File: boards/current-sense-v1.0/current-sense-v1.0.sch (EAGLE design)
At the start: 90 parts, among them IC1 ISO7241, IC2 ISO7241, IC3 ISO7242, IC4 ISO7240, J1 4-PIN_2MM-H, J2 MKS-1658, J3 8-PIN_2MM-H, J6 DF22-2, Q1 IRFH7545, Q2 IRFH7545, Q3 IRFH7545, Q4 IRFH7545, Q5 IRFH7545, Q6 IRFH7545, U1 DRV8303DCA, U13 TLV70233DBVR, U2 INA240PWR, U3 INA240PWR, U4 INA240PWR, U5 TLV70233DBVR, U6 ADS8028IRTJT, U7 MPM3620GQV-P, U8 VND5E006ASPTR-E, U9 TLV70450

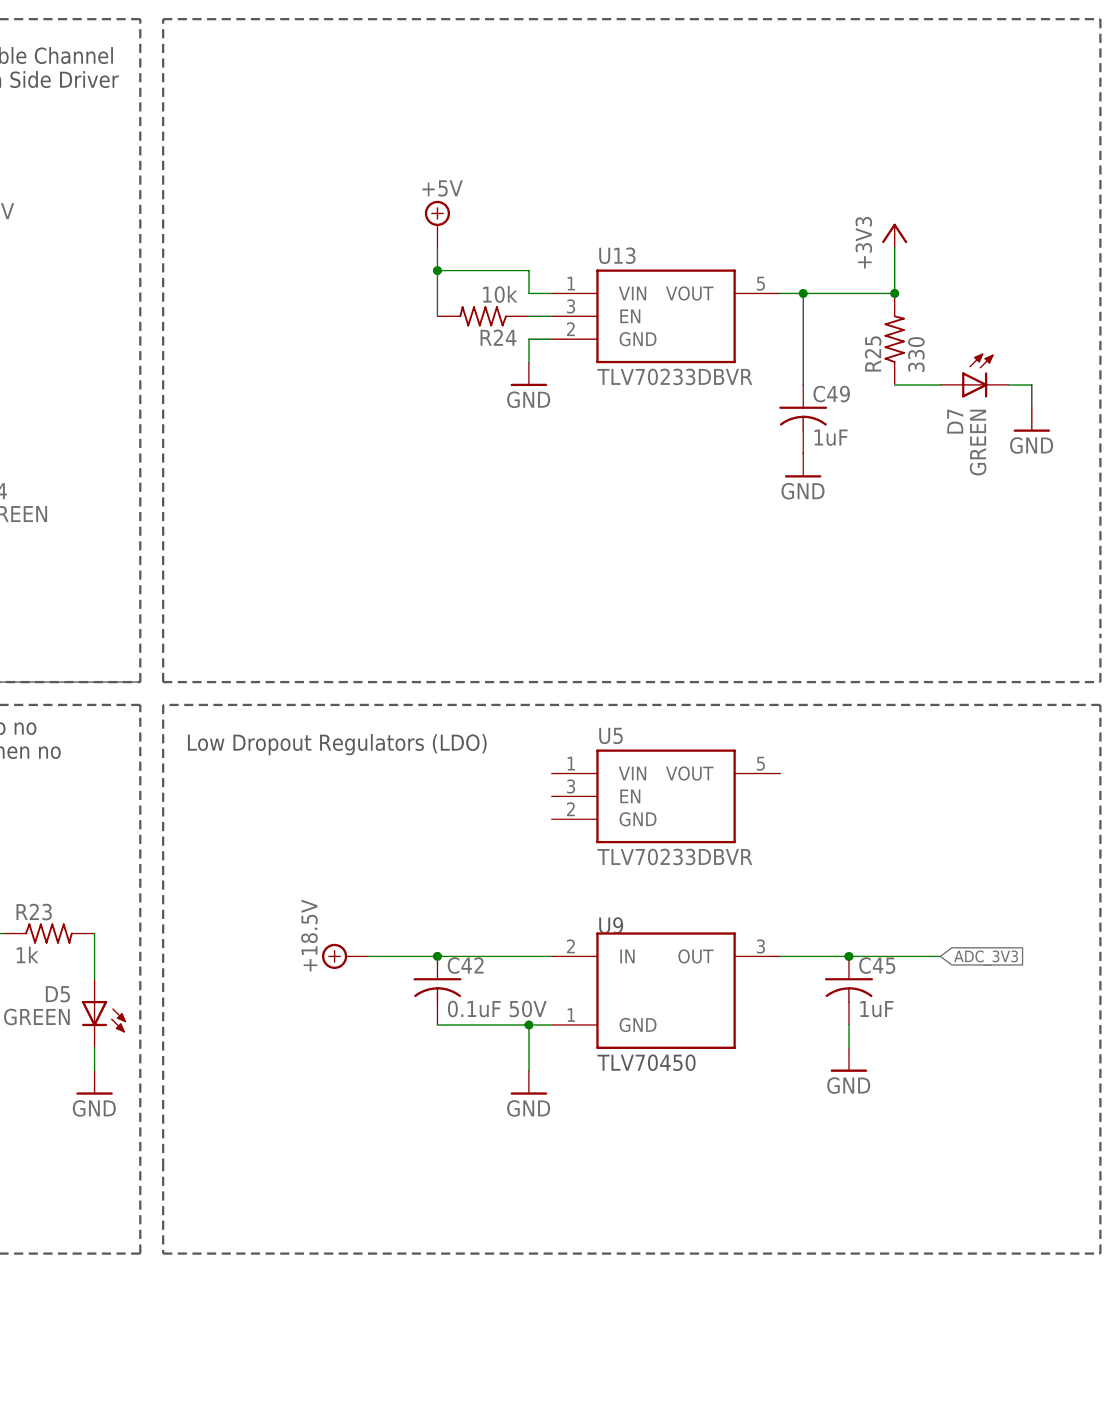
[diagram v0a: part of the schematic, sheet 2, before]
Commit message: replaced TLV 70450 with TLV 70433
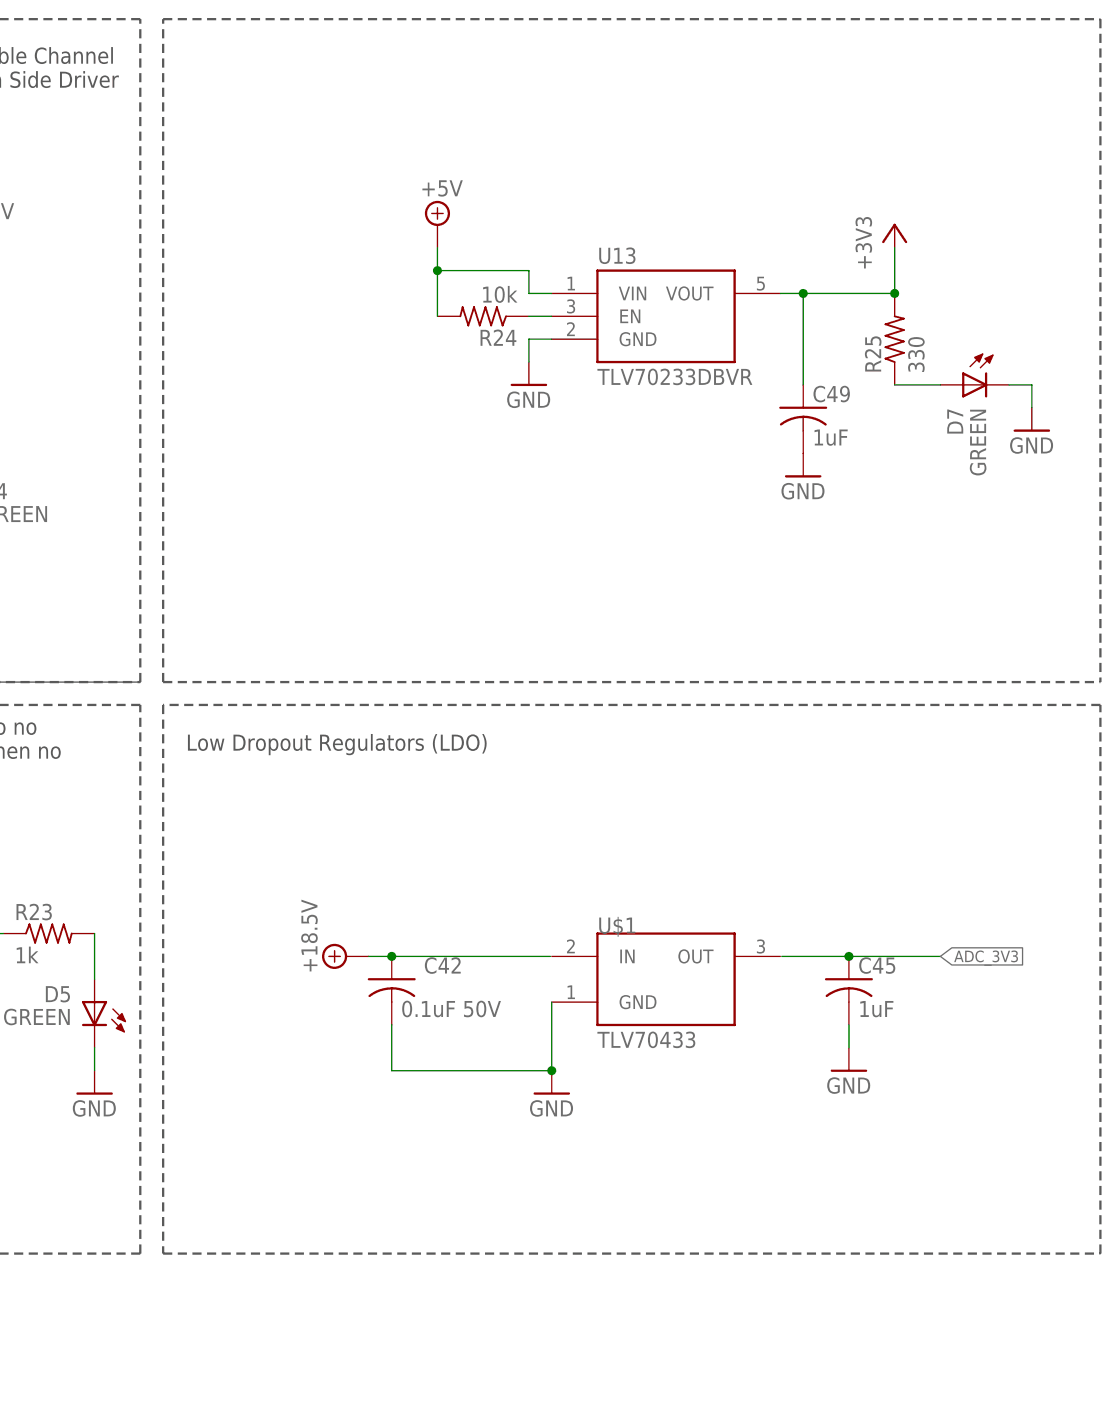
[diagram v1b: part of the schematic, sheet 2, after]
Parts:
- removed U5: TLV70233DBVR, RoboJackets-PowerICs:TLV70233DBVR
- removed U9: TLV70450, RoboJackets-PowerICs:TLV70450
- added U$1: TLV70433, RoboJackets-PowerICs:TLV70433
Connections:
- net +18.5V: no longer U9.IN
- net ADC_3V3: no longer U9.OUT
- net GND: now also U$1.GND; no longer U9.GND
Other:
- moved on the sheet: C42
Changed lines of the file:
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@@
 <part name="GND80" library="supply1" library_urn="urn:adsk.eagle:library:371" deviceset="GND" device=""/>
 <part name="SUPPLY42" library="RoboJackets-Supplies" deviceset="+18.5V" device=""/>
-<part name="U9" library="RoboJackets-PowerICs" deviceset="TLV70450" device=""/>
 <part name="C14" library="rcl" library_urn="urn:adsk.eagle:library:334" deviceset="C-US" device="C0603" package3d_urn="urn:adsk.eagle:package:23616/2" value="0.1uf"/>
 <part name="GND24" library="supply1" library_urn="urn:adsk.eagle:library:371" deviceset="GND" device=""/>
@@
 <part name="+3V13" library="supply1" library_urn="urn:adsk.eagle:library:371" deviceset="+3V3" device=""/>
 <part name="+3V14" library="supply1" library_urn="urn:adsk.eagle:library:371" deviceset="+3V3" device=""/>
-<part name="U5" library="RoboJackets-PowerICs" deviceset="TLV70233" device="DBVR"/>
+<part name="U$1" library="RoboJackets-PowerICs" deviceset="TLV70433" device=""/>
 </parts>
 <sheets>
@@
 <wire x1="162.56" y1="200.66" x2="12.7" y2="200.66" width="0.254" layer="97" style="shortdash"/>
 <wire x1="165.1" y1="200.66" x2="269.24" y2="200.66" width="0.254" layer="97" style="shortdash"/>
-<wire x1="269.24" y1="200.66" x2="269.24" y2="132.08" width="0.254" layer="97" style="shortdash"/>
+<wire x1="269.24" y1="200.66" x2="269.24" y2="127" width="0.254" layer="97" style="shortdash"/>
 <wire x1="269.24" y1="124.46" x2="165.1" y2="124.46" width="0.254" layer="97" style="shortdash"/>
 <wire x1="165.1" y1="127" x2="165.1" y2="200.66" width="0.254" layer="97" style="shortdash"/>
@@
 <wire x1="43.18" y1="50.8" x2="12.7" y2="50.8" width="0.254" layer="97" style="shortdash"/>
 <wire x1="165.1" y1="127" x2="269.24" y2="127" width="0.254" layer="97" style="shortdash"/>
-<wire x1="269.24" y1="127" x2="269.24" y2="132.08" width="0.254" layer="97" style="shortdash"/>
-<wire x1="165.1" y1="124.46" x2="165.1" y2="73.66" width="0.254" layer="97" style="shortdash"/>
-<wire x1="165.1" y1="73.66" x2="165.1" y2="63.5" width="0.254" layer="97" style="shortdash"/>
+<wire x1="165.1" y1="124.46" x2="165.1" y2="63.5" width="0.254" layer="97" style="shortdash"/>
 <text x="167.64" y="119.38" size="1.778" layer="97">Low Dropout Regulators (LDO)</text>
 <text x="142.24" y="193.04" size="1.778" layer="97">Double Channel
@@
 <attribute name="VALUE" x="193.675" y="180.975" size="1.778" layer="96"/>
 </instance>
-<instance part="GND75" gate="1" x="205.74" y="81.28" smashed="yes">
-<attribute name="VALUE" x="203.2" y="78.74" size="1.778" layer="96"/>
+<instance part="GND75" gate="1" x="208.28" y="81.28" smashed="yes">
+<attribute name="VALUE" x="205.74" y="78.74" size="1.778" layer="96"/>
 </instance>
 <instance part="C45" gate="G$1" x="241.3" y="93.98" smashed="yes">
@@
 <attribute name="VALUE" x="242.316" y="89.789" size="1.778" layer="96"/>
 </instance>
-<instance part="C42" gate="G$1" x="195.58" y="93.98" smashed="yes">
-<attribute name="NAME" x="196.596" y="94.615" size="1.778" layer="95"/>
-<attribute name="VALUE" x="196.596" y="89.789" size="1.778" layer="96"/>
+<instance part="C42" gate="G$1" x="190.5" y="93.98" smashed="yes">
+<attribute name="NAME" x="194.056" y="94.615" size="1.778" layer="95"/>
+<attribute name="VALUE" x="191.516" y="89.789" size="1.778" layer="96"/>
 </instance>
 <instance part="GND80" gate="1" x="241.3" y="83.82" smashed="yes">
@@
 <attribute name="VALUE" x="182.245" y="94.615" size="1.778" layer="96" rot="R90"/>
 </instance>
-<instance part="U9" gate="G$1" x="220.98" y="91.44" smashed="yes">
-<attribute name="NAME" x="213.36" y="99.06" size="1.778" layer="97"/>
-<attribute name="VALUE" x="213.36" y="83.82" size="1.778" layer="97"/>
-</instance>
-<instance part="U5" gate="G$1" x="220.98" y="109.22" smashed="yes">
-<attribute name="VALUE" x="213.36" y="106.68" size="1.778" layer="96"/>
-<attribute name="NAME" x="213.36" y="121.92" size="1.778" layer="95" align="top-left"/>
+<instance part="U$1" gate="G$1" x="220.98" y="96.52" smashed="yes">
+<attribute name="NAME" x="213.36" y="99.06" size="1.778" layer="95"/>
+<attribute name="VALUE" x="213.36" y="86.36" size="1.778" layer="96"/>
 </instance>
 </instances>
@@
 </segment>
 <segment>
-<wire x1="208.28" y1="88.9" x2="205.74" y2="88.9" width="0.1524" layer="91"/>
-<pinref part="GND75" gate="1" pin="GND"/>
-<pinref part="C42" gate="G$1" pin="2"/>
-<wire x1="205.74" y1="88.9" x2="205.74" y2="83.82" width="0.1524" layer="91"/>
-<wire x1="195.58" y1="88.9" x2="205.74" y2="88.9" width="0.1524" layer="91"/>
-<junction x="205.74" y="88.9"/>
-<pinref part="U9" gate="G$1" pin="GND"/>
-</segment>
-<segment>
 <pinref part="C45" gate="G$1" pin="2"/>
 <wire x1="241.3" y1="88.9" x2="241.3" y2="86.36" width="0.1524" layer="91"/>
 <pinref part="GND80" gate="1" pin="GND"/>
+</segment>
+<segment>
+<pinref part="C42" gate="G$1" pin="2"/>
+<wire x1="190.5" y1="88.9" x2="190.5" y2="83.82" width="0.1524" layer="91"/>
+<wire x1="190.5" y1="83.82" x2="208.28" y2="83.82" width="0.1524" layer="91"/>
+<pinref part="U$1" gate="G$1" pin="GND"/>
+<wire x1="208.28" y1="83.82" x2="208.28" y2="91.44" width="0.1524" layer="91"/>
+<pinref part="GND75" gate="1" pin="GND"/>
+<junction x="208.28" y="83.82"/>
 </segment>
 </net>
@@
 <segment>
 <pinref part="C42" gate="G$1" pin="1"/>
-<wire x1="208.28" y1="96.52" x2="195.58" y2="96.52" width="0.1524" layer="91"/>
-<wire x1="195.58" y1="96.52" x2="187.96" y2="96.52" width="0.1524" layer="91"/>
-<junction x="195.58" y="96.52"/>
+<wire x1="190.5" y1="96.52" x2="187.96" y2="96.52" width="0.1524" layer="91"/>
+<junction x="190.5" y="96.52"/>
 <pinref part="SUPPLY42" gate="G$1" pin="+18.5V"/>
-<pinref part="U9" gate="G$1" pin="IN"/>
+<wire x1="208.1276" y1="96.52" x2="190.5" y2="96.52" width="0.1524" layer="91"/>
 </segment>
 </net>
@@
 <net name="ADC_3V3" class="0">
 <segment>
-<wire x1="233.68" y1="96.52" x2="241.3" y2="96.52" width="0.1524" layer="91"/>
 <pinref part="C45" gate="G$1" pin="1"/>
 <junction x="241.3" y="96.52"/>
 <wire x1="241.3" y1="96.52" x2="251.46" y2="96.52" width="0.1524" layer="91"/>
 <label x="251.46" y="96.52" size="1.27" layer="95" xref="yes"/>
-<pinref part="U9" gate="G$1" pin="OUT"/>
-</segment>
-</net>
+<wire x1="233.8324" y1="96.52" x2="241.3" y2="96.52" width="0.1524" layer="91"/>
+</segment>
+</net>

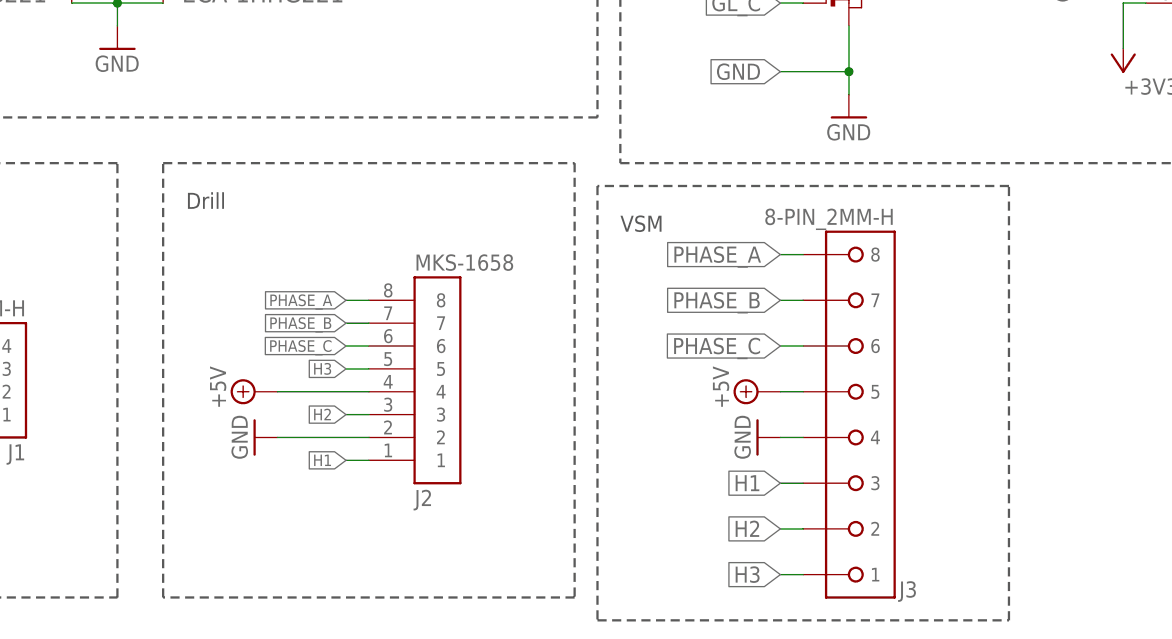
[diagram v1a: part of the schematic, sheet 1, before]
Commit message: Fixed board dimensions and some other borders
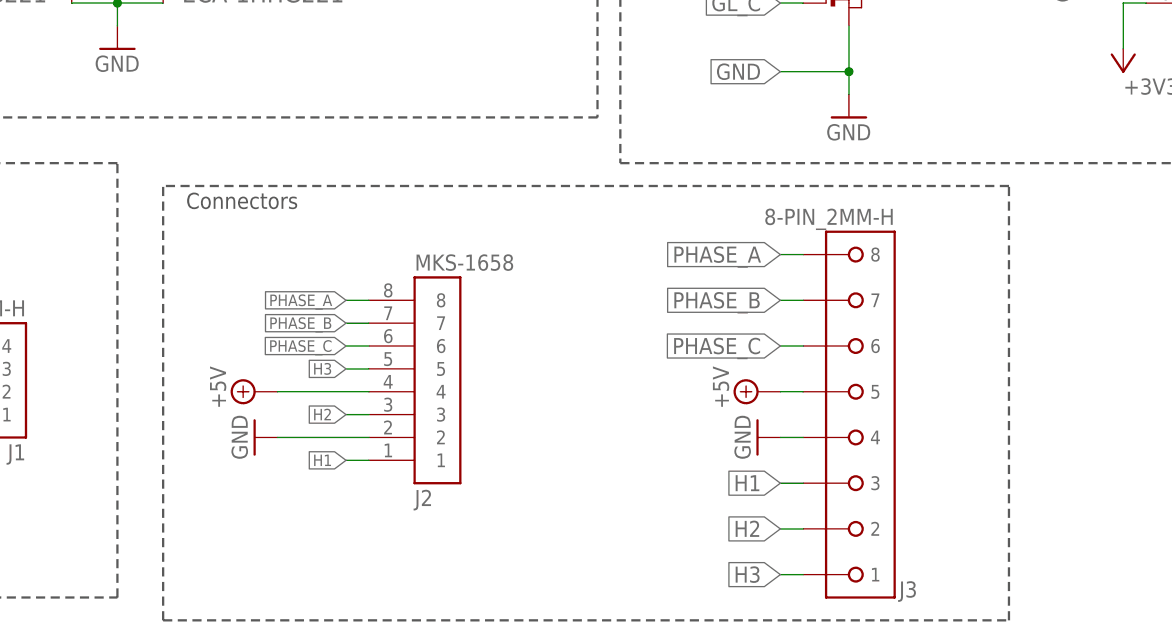
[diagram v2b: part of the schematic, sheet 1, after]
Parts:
- renumbered U$1 to U9
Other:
- note added: "Connectors"
- note removed: "Drill"
- note removed: "VSM"
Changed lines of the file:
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@@
 <part name="+3V13" library="supply1" library_urn="urn:adsk.eagle:library:371" deviceset="+3V3" device=""/>
 <part name="+3V14" library="supply1" library_urn="urn:adsk.eagle:library:371" deviceset="+3V3" device=""/>
-<part name="U$1" library="RoboJackets-PowerICs" deviceset="TLV70433" device=""/>
+<part name="U9" library="RoboJackets-PowerICs" deviceset="TLV70433" device=""/>
 </parts>
 <sheets>
@@
 <wire x1="53.34" y1="5.08" x2="53.34" y2="53.34" width="0.254" layer="97" style="shortdash"/>
 <wire x1="53.34" y1="53.34" x2="10.16" y2="53.34" width="0.254" layer="97" style="shortdash"/>
-<wire x1="58.42" y1="53.34" x2="104.14" y2="53.34" width="0.254" layer="97" style="shortdash"/>
-<wire x1="104.14" y1="53.34" x2="104.14" y2="5.08" width="0.254" layer="97" style="shortdash"/>
-<wire x1="104.14" y1="5.08" x2="58.42" y2="5.08" width="0.254" layer="97" style="shortdash"/>
-<wire x1="58.42" y1="5.08" x2="58.42" y2="53.34" width="0.254" layer="97" style="shortdash"/>
-<wire x1="106.68" y1="2.54" x2="152.4" y2="2.54" width="0.254" layer="97" style="shortdash"/>
+<wire x1="58.42" y1="2.54" x2="58.42" y2="50.8" width="0.254" layer="97" style="shortdash"/>
+<wire x1="58.42" y1="2.54" x2="152.4" y2="2.54" width="0.254" layer="97" style="shortdash"/>
 <wire x1="152.4" y1="2.54" x2="152.4" y2="50.8" width="0.254" layer="97" style="shortdash"/>
-<wire x1="152.4" y1="50.8" x2="106.68" y2="50.8" width="0.254" layer="97" style="shortdash"/>
-<wire x1="106.68" y1="50.8" x2="106.68" y2="2.54" width="0.254" layer="97" style="shortdash"/>
+<wire x1="152.4" y1="50.8" x2="58.42" y2="50.8" width="0.254" layer="97" style="shortdash"/>
 <text x="91.44" y="203.2" size="1.778" layer="97">Main Driver</text>
 <text x="12.7" y="48.26" size="1.778" layer="97">Encoder</text>
-<text x="60.96" y="48.26" size="1.778" layer="97">Drill</text>
-<text x="109.22" y="45.72" size="1.778" layer="97">VSM</text>
+<text x="60.96" y="48.26" size="1.778" layer="97">Connectors</text>
 <text x="114.3" y="203.2" size="1.778" layer="97">Half Bridges</text>
 <wire x1="109.22" y1="53.34" x2="246.38" y2="53.34" width="0.254" layer="97" style="shortdash"/>
@@
 <attribute name="VALUE" x="182.245" y="94.615" size="1.778" layer="96" rot="R90"/>
 </instance>
-<instance part="U$1" gate="G$1" x="220.98" y="96.52" smashed="yes">
+<instance part="U9" gate="G$1" x="220.98" y="96.52" smashed="yes">
 <attribute name="NAME" x="213.36" y="99.06" size="1.778" layer="95"/>
 <attribute name="VALUE" x="213.36" y="86.36" size="1.778" layer="96"/>
@@
 <wire x1="190.5" y1="88.9" x2="190.5" y2="83.82" width="0.1524" layer="91"/>
 <wire x1="190.5" y1="83.82" x2="208.28" y2="83.82" width="0.1524" layer="91"/>
-<pinref part="U$1" gate="G$1" pin="GND"/>
+<pinref part="U9" gate="G$1" pin="GND"/>
 <wire x1="208.28" y1="83.82" x2="208.28" y2="91.44" width="0.1524" layer="91"/>
 <pinref part="GND75" gate="1" pin="GND"/>

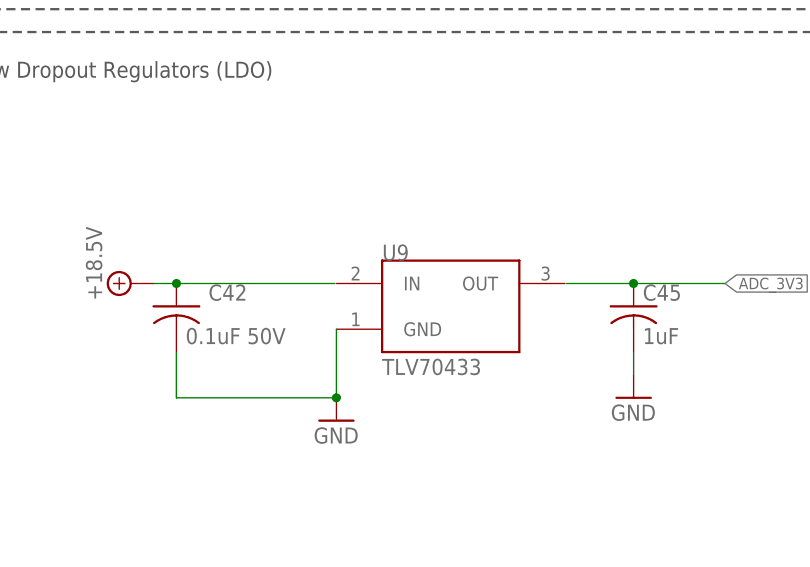
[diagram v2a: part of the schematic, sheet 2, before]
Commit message: fixed U9 LDO connections
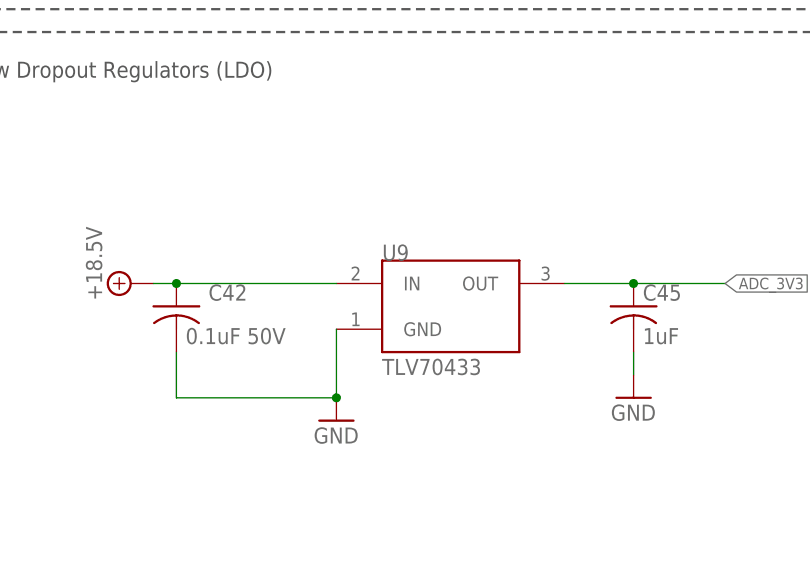
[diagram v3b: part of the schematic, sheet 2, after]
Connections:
- net +18.5V: now also U9.IN
- net ADC_3V3: now also U9.OUT
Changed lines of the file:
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@@
 <pinref part="C42" gate="G$1" pin="1"/>
 <wire x1="190.5" y1="96.52" x2="187.96" y2="96.52" width="0.1524" layer="91"/>
+<pinref part="SUPPLY42" gate="G$1" pin="+18.5V"/>
+<pinref part="U9" gate="G$1" pin="IN"/>
+<wire x1="190.5" y1="96.52" x2="208.28" y2="96.52" width="0.1524" layer="91"/>
 <junction x="190.5" y="96.52"/>
-<pinref part="SUPPLY42" gate="G$1" pin="+18.5V"/>
-<wire x1="208.1276" y1="96.52" x2="190.5" y2="96.52" width="0.1524" layer="91"/>
 </segment>
 </net>
@@
 <segment>
 <pinref part="C45" gate="G$1" pin="1"/>
-<junction x="241.3" y="96.52"/>
 <wire x1="241.3" y1="96.52" x2="251.46" y2="96.52" width="0.1524" layer="91"/>
 <label x="251.46" y="96.52" size="1.27" layer="95" xref="yes"/>
-<wire x1="233.8324" y1="96.52" x2="241.3" y2="96.52" width="0.1524" layer="91"/>
+<pinref part="U9" gate="G$1" pin="OUT"/>
+<wire x1="233.68" y1="96.52" x2="241.3" y2="96.52" width="0.1524" layer="91"/>
+<junction x="241.3" y="96.52"/>
 </segment>
 </net>
